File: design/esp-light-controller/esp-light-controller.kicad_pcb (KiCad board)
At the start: 4 copper layers, 50 x 57.6 mm, 42 parts, among them J1 LED0, J2 LED1, J3 LED2, J4 UART, P1 USB_C_Plug_USB2.0, Q1 2N7002, Q2 2N7002, Q3 2N7002, Q4 2N7002, Q5 2N7002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

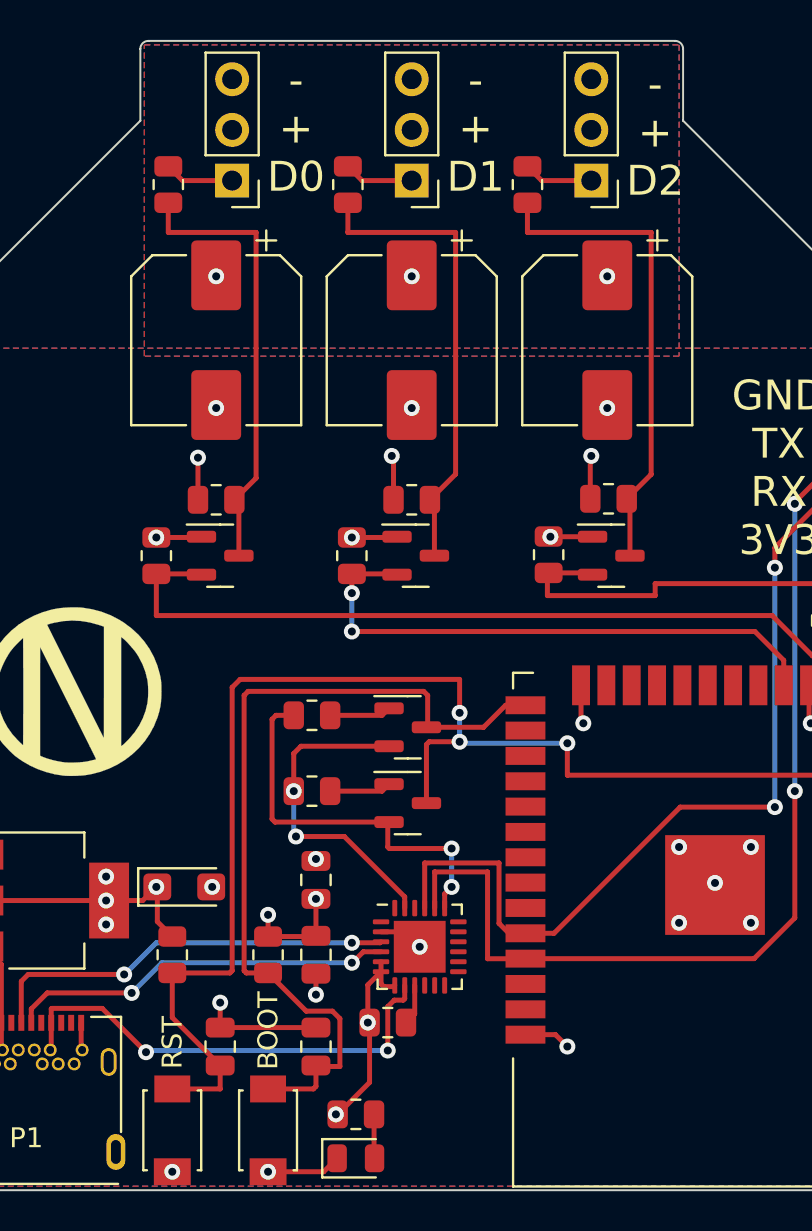
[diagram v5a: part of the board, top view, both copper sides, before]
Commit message: Restore silkscreen part references
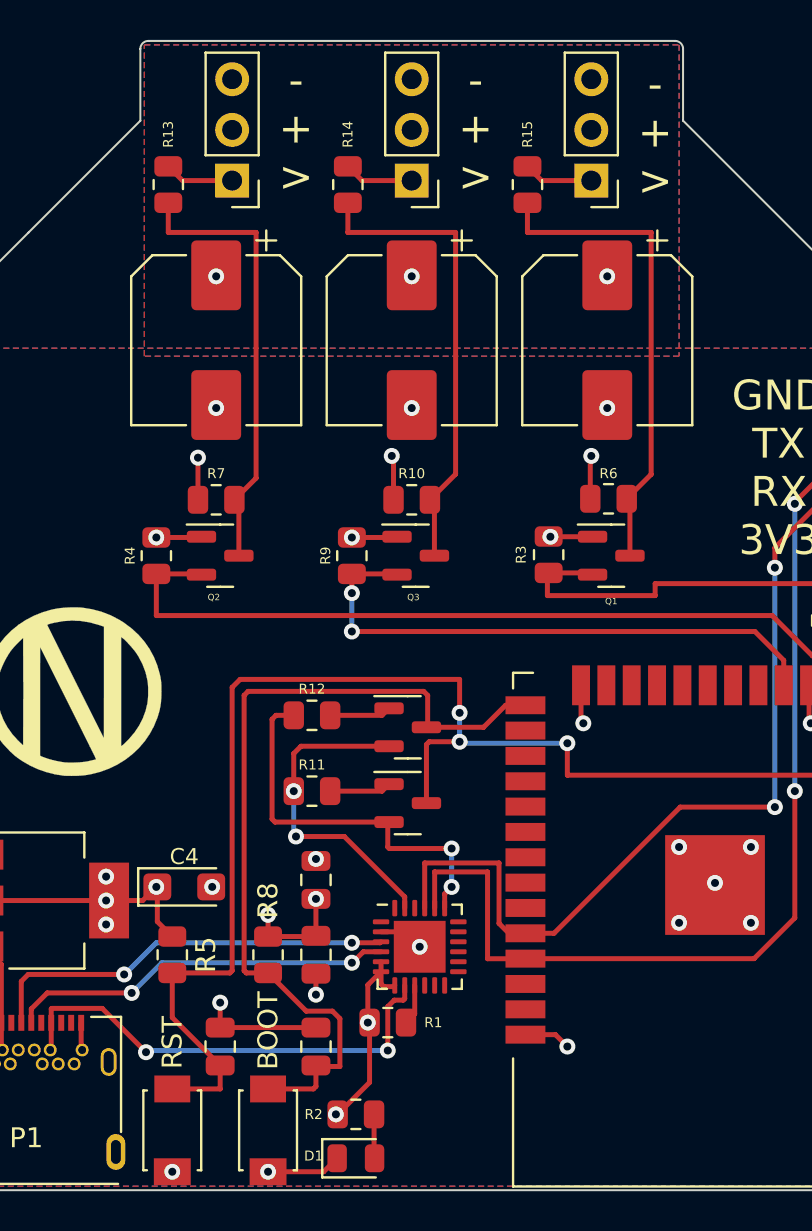
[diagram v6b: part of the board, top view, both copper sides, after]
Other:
- board text added: "- + >"
- board text removed: "- + D0"
- board text removed: "- + D1"
- board text removed: "- + D2"
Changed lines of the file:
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@@
       (effects (font (size 1 1) (thickness 0.15)))
     )
-    (fp_text user "${REFERENCE}" (at 0 0) (layer "F.Fab")
+    (fp_text user "${REFERENCE}" (at 0 -1.317157) (layer "F.SilkS")
       (effects (font (size 0.5 0.5) (thickness 0.08)))
     )
@@
       (effects (font (size 1 1) (thickness 0.15)))
     )
-    (fp_text user "${REFERENCE}" (at 0 0) (layer "F.Fab")
+    (fp_text user "${REFERENCE}" (at 2.282843 0) (layer "F.SilkS")
       (effects (font (size 0.5 0.5) (thickness 0.08)))
     )
@@
       (effects (font (size 1 1) (thickness 0.15)))
     )
-    (fp_text user "${REFERENCE}" (at 0 0) (layer "F.Fab")
+    (fp_text user "${REFERENCE}" (at -0.117157 2.082843) (layer "F.SilkS")
       (effects (font (size 0.32 0.32) (thickness 0.05)))
     )
@@
     (property "Sheetname" "")
     (attr smd)
-    (fp_text reference "R5" (at 0 0 90) (layer "F.SilkS") hide
+    (fp_text reference "R5" (at 0 -1.682843 90) (layer "F.SilkS")
       (effects (font (size 1 1) (thickness 0.15)))
     )
@@
       (effects (font (size 1 1) (thickness 0.15)))
     )
-    (fp_text user "${REFERENCE}" (at 0 0 90) (layer "F.Fab")
+    (fp_text user "${REFERENCE}" (at 2.517157 0 90) (layer "F.SilkS")
       (effects (font (size 0.5 0.5) (thickness 0.08)))
     )
@@
       (effects (font (size 1 1) (thickness 0.15)))
     )
-    (fp_text user "${REFERENCE}" (at 0 0) (layer "F.Fab")
+    (fp_text user "${REFERENCE}" (at 0 -1.517157) (layer "F.SilkS")
       (effects (font (size 0.8 0.8) (thickness 0.12)))
     )
@@
       (effects (font (size 1 1) (thickness 0.15)))
     )
-    (fp_text user "${REFERENCE}" (at 0 0 90) (layer "F.Fab")
+    (fp_text user "${REFERENCE}" (at 0 1.379657 90) (layer "F.SilkS")
       (effects (font (size 0.5 0.5) (thickness 0.08)))
     )
@@
       (effects (font (size 1 1) (thickness 0.15)))
     )
-    (fp_text user "${REFERENCE}" (at 0 0) (layer "F.Fab")
+    (fp_text user "${REFERENCE}" (at 0 -1.317157) (layer "F.SilkS")
       (effects (font (size 0.5 0.5) (thickness 0.08)))
     )
@@
       (effects (font (size 1 1) (thickness 0.15)))
     )
-    (fp_text value "CP2104" (at 0 0) (layer "F.Fab")
+    (fp_text value "CP2104" (at 0.082843 0) (layer "F.Fab")
       (effects (font (size 1 1) (thickness 0.15)))
     )
@@
       (effects (font (size 1 1) (thickness 0.15)))
     )
-    (fp_text user "${REFERENCE}" (at 0 0) (layer "F.Fab")
+    (fp_text user "${REFERENCE}" (at 0 -1.317157) (layer "F.SilkS")
       (effects (font (size 0.5 0.5) (thickness 0.08)))
     )
@@
       (effects (font (size 1 1) (thickness 0.15)))
     )
-    (fp_text user "${REFERENCE}" (at 0 0) (layer "F.Fab")
+    (fp_text user "${REFERENCE}" (at 0 2.282843) (layer "F.SilkS")
       (effects (font (size 0.32 0.32) (thickness 0.05)))
     )
@@
       (effects (font (size 1 1) (thickness 0.15)))
     )
-    (fp_text user "${REFERENCE}" (at 0 0) (layer "F.Fab")
+    (fp_text user "${REFERENCE}" (at -2.117157 0) (layer "F.SilkS")
       (effects (font (size 0.5 0.5) (thickness 0.08)))
     )
@@
       (effects (font (size 1 1) (thickness 0.15)))
     )
-    (fp_text user "${REFERENCE}" (at 0 0) (layer "F.Fab")
+    (fp_text user "${REFERENCE}" (at 0 -1.267157) (layer "F.SilkS")
       (effects (font (size 0.5 0.5) (thickness 0.08)))
     )
@@
     (property "Sheetname" "")
     (attr smd)
-    (fp_text reference "R8" (at 0 0 90) (layer "F.SilkS") hide
+    (fp_text reference "R8" (at -2.717157 0 90) (layer "F.SilkS")
       (effects (font (size 1 1) (thickness 0.15)))
     )
@@
       (effects (font (size 1 1) (thickness 0.15)))
     )
-    (fp_text user "${REFERENCE}" (at 0 0 90) (layer "F.Fab")
+    (fp_text user "${REFERENCE}" (at 0 1.317157 90) (layer "F.SilkS")
       (effects (font (size 0.5 0.5) (thickness 0.08)))
     )
@@
       (effects (font (size 1 1) (thickness 0.15)))
     )
-    (fp_text user "${REFERENCE}" (at 0 0 90) (layer "F.Fab")
+    (fp_text user "${REFERENCE}" (at 2.517157 0 90) (layer "F.SilkS")
       (effects (font (size 0.5 0.5) (thickness 0.08)))
     )
@@
       (effects (font (size 1 1) (thickness 0.15)))
     )
-    (fp_text user "${REFERENCE}" (at 0 0 90) (layer "F.Fab")
+    (fp_text user "${REFERENCE}" (at 0 1.317157 90) (layer "F.SilkS")
       (effects (font (size 0.5 0.5) (thickness 0.08)))
     )
@@
       (effects (font (size 1 1) (thickness 0.15)))
     )
-    (fp_text user "${REFERENCE}" (at 0 0) (layer "F.Fab")
+    (fp_text user "${REFERENCE}" (at -0.317157 2.082843) (layer "F.SilkS")
       (effects (font (size 0.32 0.32) (thickness 0.05)))
     )
@@
       (effects (font (size 1 1) (thickness 0.15)))
     )
-    (fp_text user "${REFERENCE}" (at 0 0 90) (layer "F.Fab")
+    (fp_text user "${REFERENCE}" (at 2.517157 0 90) (layer "F.SilkS")
       (effects (font (size 0.5 0.5) (thickness 0.08)))
     )
@@
       (effects (font (size 1 1) (thickness 0.15)))
     )
-    (fp_text user "${REFERENCE}" (at 0 -0.05) (layer "F.Fab")
+    (fp_text user "${REFERENCE}" (at 0 -1.317157) (layer "F.SilkS")
       (effects (font (size 0.5 0.5) (thickness 0.08)))
     )
@@
       (effects (font (size 1 1) (thickness 0.15)))
     )
-    (fp_text user "${REFERENCE}" (at 0 0) (layer "F.Fab")
+    (fp_text user "${REFERENCE}" (at -2.117157 -0.117157) (layer "F.SilkS")
       (effects (font (size 0.5 0.5) (thickness 0.08)))
     )
@@
     (effects (font (size 1.5 1.5) (thickness 0.2)))
   )
-  (gr_text "-\n+\nD1" (at 143.277157 52.387157) (layer "F.SilkS")
+  (gr_text "-\n+\n>" (at 143.277157 52.387157) (layer "F.SilkS")
     (effects (font (size 1.5 1.5) (thickness 0.2)))
   )
-  (gr_text "-\n+\nD2" (at 152.277157 52.587157) (layer "F.SilkS")
+  (gr_text "-\n+\n>" (at 152.277157 52.587157) (layer "F.SilkS")
     (effects (font (size 1.5 1.5) (thickness 0.2)))
   )
-  (gr_text "-\n+\nD0" (at 134.277157 52.387157) (layer "F.SilkS")
+  (gr_text "-\n+\n>" (at 134.277157 52.387157) (layer "F.SilkS")
     (effects (font (size 1.5 1.5) (thickness 0.2)))
   )

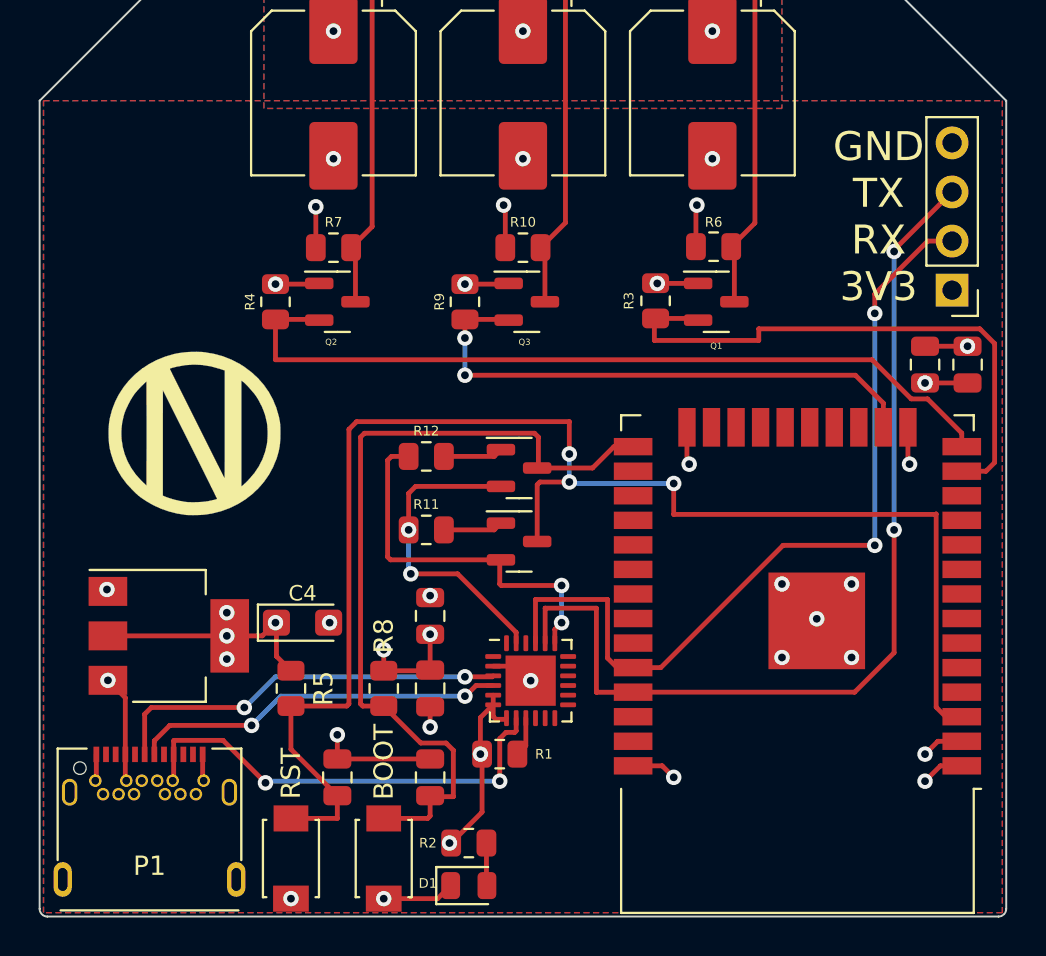
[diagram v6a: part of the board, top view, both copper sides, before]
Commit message: Resolves #39, #40, #43. Rev D.
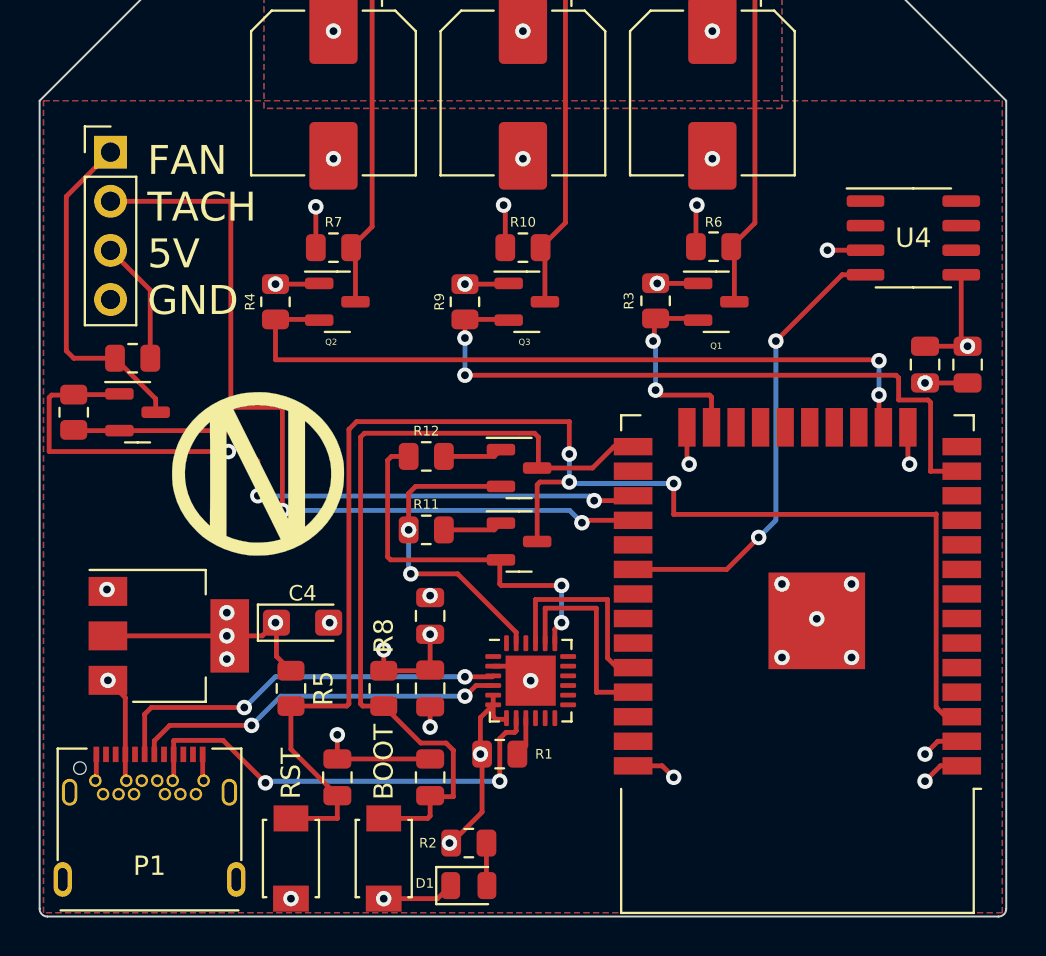
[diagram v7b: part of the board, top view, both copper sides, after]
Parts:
- added Q6: 2N7002, Package_TO_SOT_SMD:SOT-23, F.Cu at (120.1, 79.5)
- added R16: 10k, Resistor_SMD:R_0805_2012Metric, F.Cu at (116.8, 79.5)
- added R17: 10k, Resistor_SMD:R_0805_2012Metric, F.Cu at (119.9, 76.7)
- added U4: DS18B20Z, Package_SO:SOIC-8_3.9x4.9mm_P1.27mm, F.Cu at (160.3, 70.5)
- J4: value UART -> PWM_FAN
- moved J4 44.1 mm to (118.7, 66.0), turned to 0 degrees
- moved G*** 3.90 mm to (126.4, 82.7)
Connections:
- J4 pad 1: +3V3 -> /fan
- J4 pad 2: /esp_rx -> /tach
- J4 pad 3: /esp_tx -> +5V
- U3 pad 13: /ledctl2 -> /ledctl1
- U3 pad 14: /ledctl0 -> GND
- U3 pad 16: /ledctl1 -> /ledctl0
- U3 pad 23: unconnected-(U3-Pad23) -> /ledctl2
- U3 pad 27: unconnected-(U3-Pad27) -> /fanctl
- U3 pad 28: unconnected-(U3-Pad28) -> /tach
- U3 pad 30: unconnected-(U3-Pad30) -> Net-(U3-Pad30)
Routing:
- net /tach: track 0.00 -> 43.4 mm, vias 0 -> 2
- net /esp_tx: track 50.1 -> 10.7 mm, vias 2 -> 0
- net /esp_rx: track 43.8 -> 10.5 mm, vias 2 -> 0
- net /fanctl: track 0.00 -> 31.6 mm, vias 0 -> 2
- net Net-(U3-Pad30): track 0.00 -> 23.8 mm, vias 0 -> 2
- net /ledctl2: track 30.0 -> 10.7 mm, vias 0 -> 2
- net +3V3: track 38.3 -> 56.0 mm, vias 13 -> 15
- net /fan: track 0.00 -> 17.6 mm
- net /ledctl1: track 28.7 -> 35.7 mm
- net +5V: track 35.9 -> 42.3 mm
- net GND: track 26.5 -> 30.4 mm
- net /ledctl0: track 42.1 -> 39.1 mm, vias 0 -> 2
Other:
- board text added: "FAN TACH 5V GND"
- board text added: "helios :: Rev D nnarain"
- board text removed: "GND TX RX 3V3"
- board text removed: "esp-light-controller :: Rev C nnarain"

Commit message: M3 mounting holes
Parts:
- added REF**: M3, MountingHole:MountingHole_3.2mm_M3_DIN965, F.Cu at (121.0, 63.4)
- added REF**: M3, MountingHole:MountingHole_3.2mm_M3_DIN965, F.Cu at (159.1, 63.4)
- moved J4 2.54 mm to (118.7, 68.6)
- moved Q6 2.54 mm to (120.1, 82.0)
- moved R16 2.54 mm to (116.8, 82.0)
- moved R17 2.54 mm to (119.9, 79.2)
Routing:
- net /tach: track 43.4 -> 36.7 mm
- net /fanctl: track 31.6 -> 30.1 mm
- net +3V3: track 56.0 -> 56.3 mm, vias 15 -> 14
